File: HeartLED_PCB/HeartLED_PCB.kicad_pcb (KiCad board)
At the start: 2 copper layers, 58.8 x 52.2 mm, 38 parts, among them U1 ICM7555IBAZ-T, U2 CD4017BM96, U3 HT7750A, U4 HX SS12F44G4

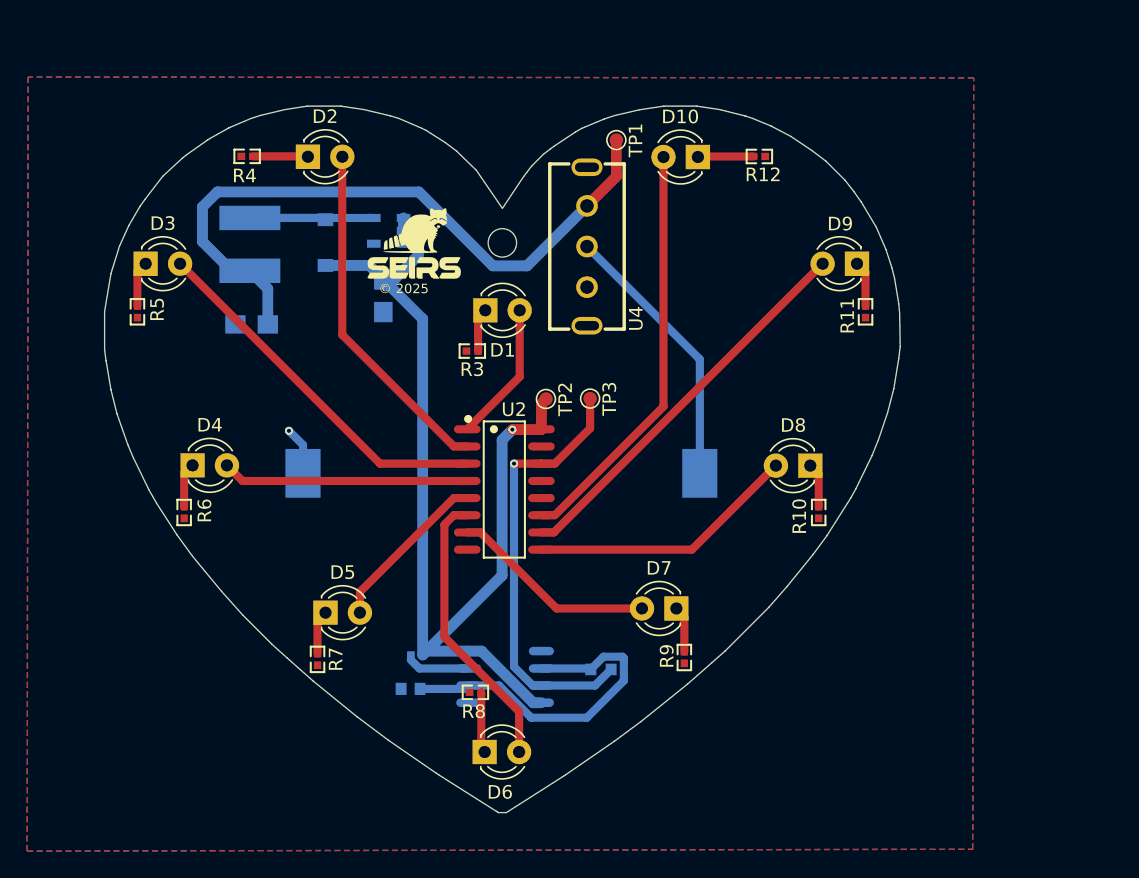
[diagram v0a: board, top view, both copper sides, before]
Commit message: Changed DC-DC Boost Converter
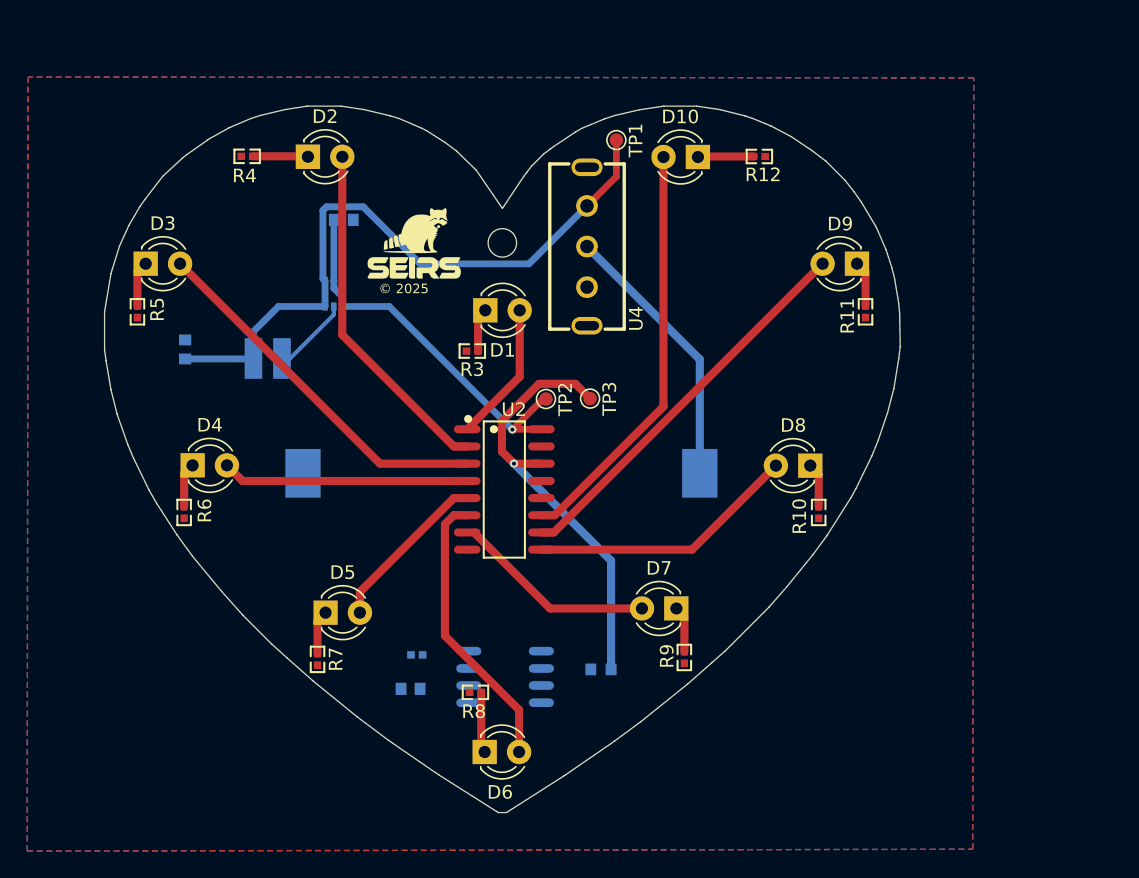
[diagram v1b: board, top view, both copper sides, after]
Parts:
- removed S1: 1N5817, FOOTPRINTS:1N5817W
- C2: value 47uF(Tantalum) -> 10uF; footprint FOOTPRINTS:TAJA476K006RNJ -> FOOTPRINTS:CL10A106MQ8NNNC
- C3: value 22uF(Tantalum) -> 10uF; footprint FOOTPRINTS:TAJA226M010RNJ -> FOOTPRINTS:CL10A106MQ8NNNC
- L1: value 47-100uH -> 4.7uH; footprint FOOTPRINTS:SMNR5040-470MT -> FOOTPRINTS:LQH3NPN4R7MMEL
- U3: value HT7750A -> TPS61222DCKR; footprint FOOTPRINTS:HT7750A -> FOOTPRINTS:TPS61222DCKR
- moved L1 8.53 mm to (112.7, 91.1), turned to 0 degrees
- moved C3 6.32 mm to (118.3, 80.9), turned to 0 degrees
- moved U3 6.16 mm to (117.6, 86.4), turned to 90 degrees
- moved C2 5.25 mm to (106.6, 90.5), turned to 90 degrees
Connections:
- U3 pad 1: +5V -> +3V
- U3 pad 3: unconnected-(U3-NC-Pad3) -> GND
- U3 pad 4: GND -> +5V
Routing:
- net +5V: track 74.7 -> 28.3 mm
- net Net-(U1-THRESHOLD): track 25.4 -> 0.00 mm
- net Net-(U3-L): track 14.6 -> 5.78 mm
- net Net-(U1-DISCHARGE): track 4.55 -> 0.00 mm
- net GND: track 3.57 -> 0.00 mm, vias 1 -> 0
- net Net-(D7-A): track 15.2 -> 14.7 mm

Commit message: Cleanup
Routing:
- net +5V: track 28.3 -> 69.5 mm
- net Net-(U1-THRESHOLD): track 0.00 -> 25.1 mm
- net Net-(U1-DISCHARGE): track 0.00 -> 5.06 mm
- net ASTABLE_OUTPUT: track 31.8 -> 36.8 mm
- net GND: track 0.00 -> 3.91 mm, vias 0 -> 1

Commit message: Cleanup
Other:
- board text added: "v1.0.0"
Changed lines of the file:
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@@
+		)
+	)
+	(gr_text "v1.0.0"
+		(at 113.34 83.12 0)
+		(layer "B.SilkS")
+		(effects
+			(font
+				(face "Liberation Mono")
+				(size 0.8 0.8)
+				(thickness 0.1)
+			)
+			(justify left mirror)
+		)
+		(render_cache "v1.0.0" 0
+			(polygon
+				(pts
+					(xy 112.947062 83.452) (xy 113.064103 83.452) (xy 113.302093 82.851748) (xy 113.191109 82.851748)
+					(xy 113.043782 83.242732) (xy 113.034403 83.272237) (xy 113.005875 83.374428) (xy 112.986727 83.309362)
+					(xy 112.965233 83.243905) (xy 112.813607 82.851748) (xy 112.703014 82.851748)
+				)
+			)
+			(polygon
+				(pts
+					(xy 112.581479 83.452) (xy 112.581479 83.372279) (xy 112.340362 83.372279) (xy 112.340362 82.814819)
+					(xy 112.366096 82.847622) (xy 112.398443 82.870398) (xy 112.436887 82.889069) (xy 112.474745 82.902832)
+					(xy 112.516984 82.913615) (xy 112.558853 82.919421) (xy 112.586559 82.920527) (xy 112.586559 82.839243)
+					(xy 112.546479 82.837033) (xy 112.507522 82.830401) (xy 112.469689 82.819349) (xy 112.432979 82.803877)
+					(xy 112.395775 82.782405) (xy 112.362558 82.755103) (xy 112.337889 82.724176) (xy 112.332156 82.714191)
+					(xy 112.240907 82.714191) (xy 112.240907 83.372279) (xy 112.04688 83.372279) (xy 112.04688 83.452)
+				)
+			)
+			(polygon
+				(pts
+					(xy 111.723112 83.452) (xy 111.723112 83.289431) (xy 111.593956 83.289431) (xy 111.593956 83.452)
+				)
+			)
+			(polygon
+				(pts
+					(xy 111.050956 83.151874) (xy 110.9218 83.151874) (xy 110.9218 83.014316) (xy 111.050956 83.014316)
+				)
+			)
+			(polygon
+				(pts
+					(xy 111.010134 82.70252) (xy 111.049905 82.707621) (xy 111.09282 82.719862) (xy 111.130487 82.73878)
+					(xy 111.162906 82.764375) (xy 111.190076 82.796647) (xy 111.208877 82.828679) (xy 111.224492 82.865424)
+					(xy 111.236919 82.906883) (xy 111.246161 82.953054) (xy 111.251259 82.993385) (xy 111.254318 83.036732)
+					(xy 111.255338 83.083095) (xy 111.254749 83.1173) (xy 111.252131 83.16047) (xy 111.247419 83.200855)
+					(xy 111.238583 83.247422) (xy 111.226475 83.289638) (xy 111.211094 83.327503) (xy 111.188318 83.367198)
+					(xy 111.175168 83.384588) (xy 111.145364 83.414236) (xy 111.110889 83.437042) (xy 111.071743 83.453007)
+					(xy 111.027926 83.462129) (xy 110.987843 83.464505) (xy 110.971392 83.464122) (xy 110.925097 83.458386)
+					(xy 110.883391 83.445767) (xy 110.846274 83.426265) (xy 110.813745 83.39988) (xy 110.785806 83.366612)
+					(xy 110.766104 83.333827) (xy 110.749742 83.296778) (xy 110.736718 83.255464) (xy 110.727035 83.209885)
+					(xy 110.721692 83.170351) (xy 110.718486 83.128088) (xy 110.717418 83.083095) (xy 110.81785 83.083095)
+					(xy 110.818009 83.101864) (xy 110.819795 83.1461) (xy 110.823565 83.186501) (xy 110.83071 83.22992)
+					(xy 110.842656 83.273595) (xy 110.858492 83.309752) (xy 110.875382 83.334919) (xy 110.906898 83.362907)
+					(xy 110.945833 83.379178) (xy 110.986671 83.383807) (xy 111.017974 83.381272) (xy 111.05867 83.367965)
+					(xy 111.091854 83.34325) (xy 111.115045 83.311706) (xy 111.122238 83.297446) (xy 111.136271 83.2584)
+					(xy 111.145233 83.218503) (xy 111.151365 83.172671) (xy 111.154313 83.129944) (xy 111.155296 83.083095)
+					(xy 111.15514 83.063372) (xy 111.153389 83.017155) (xy 111.149691 82.975357) (xy 111.142684 82.931029)
+					(xy 111.132875 82.893062) (xy 111.115436 82.852334) (xy 111.098681 82.828429) (xy 111.066775 82.801845)
+					(xy 111.026739 82.786389) (xy 110.984326 82.781993) (xy 110.957769 82.783729) (xy 110.916146 82.795606)
+					(xy 110.882468 82.818735) (xy 110.856734 82.853116) (xy 110.84762 82.872225) (xy 110.834596 82.912292)
+					(xy 110.826394 82.953348) (xy 110.821647 82.992294) (xy 110.818799 83.035543) (xy 110.81785 83.083095)
+					(xy 110.717418 83.083095) (xy 110.717989 83.048312) (xy 110.720531 83.00451) (xy 110.725106 82.963652)
+					(xy 110.733684 82.916717) (xy 110.745439 82.874381) (xy 110.760371 82.836643) (xy 110.782484 82.797429)
+					(xy 110.795316 82.780318) (xy 110.824771 82.751147) (xy 110.859283 82.728707) (xy 110.89885 82.712999)
+					(xy 110.943473 82.704023) (xy 110.984521 82.701685)
+				)
+			)
+			(polygon
+				(pts
+					(xy 110.378799 83.452) (xy 110.378799 83.289431) (xy 110.249644 83.289431) (xy 110.249644 83.452)
+				)
+			)
+			(polygon
+				(pts
+					(xy 109.706643 83.151874) (xy 109.577487 83.151874) (xy 109.577487 83.014316) (xy 109.706643 83.014316)
+				)
+			)
+			(polygon
+				(pts
+					(xy 109.665821 82.70252) (xy 109.705593 82.707621) (xy 109.748508 82.719862) (xy 109.786174 82.73878)
+					(xy 109.818593 82.764375) (xy 109.845764 82.796647) (xy 109.864565 82.828679) (xy 109.880179 82.865424)
+					(xy 109.892607 82.906883) (xy 109.901848 82.953054) (xy 109.906946 82.993385) (xy 109.910006 83.036732)
+					(xy 109.911025 83.083095) (xy 109.910436 83.1173) (xy 109.907818 83.16047) (xy 109.903106 83.200855)
+					(xy 109.89427 83.247422) (xy 109.882162 83.289638) (xy 109.866781 83.327503) (xy 109.844005 83.367198)
+					(xy 109.830855 83.384588) (xy 109.801051 83.414236) (xy 109.766576 83.437042) (xy 109.72743 83.453007)
+					(xy 109.683613 83.462129) (xy 109.643531 83.464505) (xy 109.627079 83.464122) (xy 109.580785 83.458386)
+					(xy 109.539079 83.445767) (xy 109.501961 83.426265) (xy 109.469433 83.39988) (xy 109.441493 83.366612)
+					(xy 109.421791 83.333827) (xy 109.405429 83.296778) (xy 109.392406 83.255464) (xy 109.382722 83.209885)
+					(xy 109.377379 83.170351) (xy 109.374173 83.128088) (xy 109.373105 83.083095) (xy 109.473538 83.083095)
+					(xy 109.473696 83.101864) (xy 109.475482 83.1461) (xy 109.479253 83.186501) (xy 109.486397 83.22992)
+					(xy 109.498343 83.273595) (xy 109.51418 83.309752) (xy 109.531069 83.334919) (xy 109.562585 83.362907)
+					(xy 109.601521 83.379178) (xy 109.642358 83.383807) (xy 109.673662 83.381272) (xy 109.714357 83.367965)
+					(xy 109.747541 83.34325) (xy 109.770732 83.311706) (xy 109.777926 83.297446) (xy 109.791958 83.2584)
+					(xy 109.800921 83.218503) (xy 109.807053 83.172671) (xy 109.810001 83.129944) (xy 109.810983 83.083095)
+					(xy 109.810828 83.063372) (xy 109.809076 83.017155) (xy 109.805378 82.975357) (xy 109.798371 82.931029)
+					(xy 109.788562 82.893062) (xy 109.771123 82.852334) (xy 109.754369 82.828429) (xy 109.722462 82.801845)
+					(xy 109.682426 82.786389) (xy 109.640013 82.781993) (xy 109.613457 82.783729) (xy 109.571834 82.795606)
+					(xy 109.538155 82.818735) (xy 109.512421 82.853116) (xy 109.503308 82.872225) (xy 109.490283 82.912292)
+					(xy 109.482081 82.953348) (xy 109.477335 82.992294) (xy 109.474487 83.035543) (xy 109.473538 83.083095)
+					(xy 109.373105 83.083095) (xy 109.373677 83.048312) (xy 109.376218 83.00451) (xy 109.380793 82.963652)
+					(xy 109.389371 82.916717) (xy 109.401127 82.874381) (xy 109.416059 82.836643) (xy 109.438171 82.797429)
+					(xy 109.451003 82.780318) (xy 109.480459 82.751147) (xy 109.51497 82.728707) (xy 109.554538 82.712999)
+					(xy 109.599161 82.704023) (xy 109.640209 82.701685)
+				)
+			)
 		)
 	)

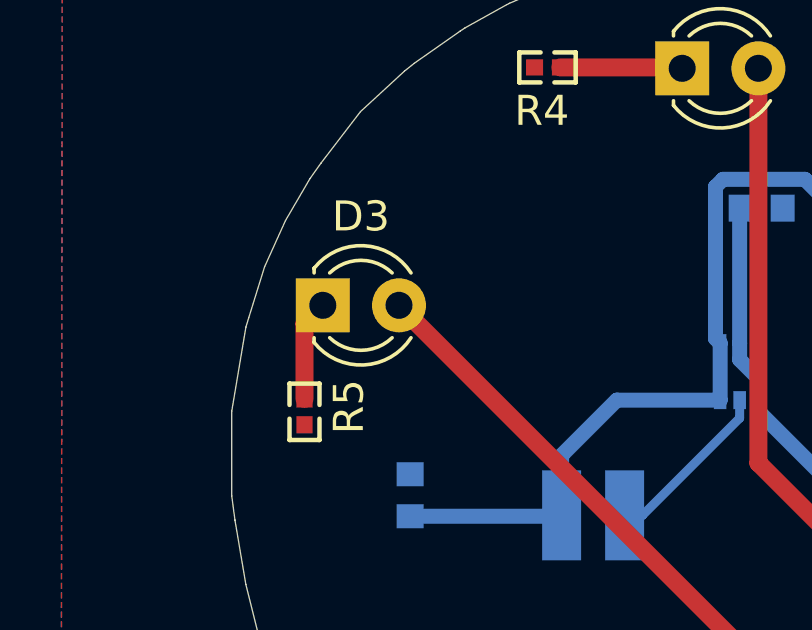
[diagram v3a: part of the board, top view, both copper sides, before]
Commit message: Changed DC-DC Boost Converter
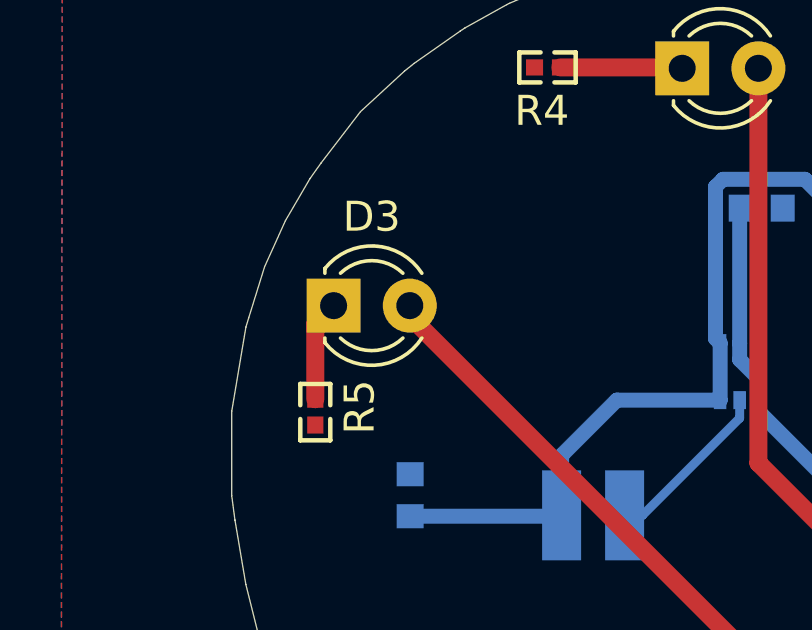
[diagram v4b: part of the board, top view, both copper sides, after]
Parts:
- moved D3 0.36 mm to (104.0, 84.2)
- moved R5 0.36 mm to (103.4, 87.7)
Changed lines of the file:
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@@
 	(footprint "LED_THT:LED_D3.0mm"
 		(layer "F.Cu")
-		(at 103.66 84.14)
+		(at 104.02 84.15)
 		(descr "LED, diameter 3.0mm, 2 pins, generated by kicad-footprint-generator")
 		(tags "LED")
@@
 	(footprint "FOOTPRINTS:0402WGJ0332TCE"
 		(layer "F.Cu")
-		(at 103.05 87.69 -90)
+		(at 103.41 87.7 -90)
 		(property "Reference" "R5"
 			(at -0.17 -1.48 90)
@@
 	)
 	(segment
-		(start 103.05 87.26)
-		(end 103.05 84.75)
+		(start 103.41 87.27)
+		(end 103.41 84.76)
 		(width 0.6)
 		(layer "F.Cu")
@@
 	)
 	(segment
-		(start 103.05 84.75)
-		(end 103.66 84.14)
+		(start 103.41 84.76)
+		(end 104.02 84.15)
 		(width 0.6)
 		(layer "F.Cu")

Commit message: Ready to route
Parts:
- removed C3: 10uF, FOOTPRINTS:CL10A106MQ8NNNC
- removed G***: LOGO, FOOTPRINTS:seirslogo
- removed G***: LOGO, FOOTPRINTS:raccoonimage
- removed H1: MountingHole, MountingHole:MountingHole_2.1mm
- removed L1: 4.7uH, FOOTPRINTS:LQH3NPN4R7MMEL
- removed R12: 3.3k, FOOTPRINTS:0402WGJ0332TCE
- removed TP2, TP3: TestPoint, TestPoint:TestPoint_Pad_D1.0mm
- removed U3: TPS61222DCKR, FOOTPRINTS:TPS61222DCKR
- removed U4: HX SS12F44G4, FOOTPRINTS:HX SS12F44G4
- added J1: Conn_01x03, Connector_PinHeader_2.54mm:PinHeader_1x03_P2.54mm_Vertical, F.Cu at (152.9, 102.6)
- added SW1: TS-1187A-B-A-B, FOOTPRINTS:TS-1187A-B-A-B, F.Cu at (150.7, 76.7)
- BT1: value Battery_Cell -> CR2032-BS-6-1; footprint Battery:BatteryHolder_Keystone_1060_1x2032 -> FOOTPRINTS:CR2032-BS-6-1; moved to F.Cu
- C1: value 4.7uF -> 100nF; footprint FOOTPRINTS:CL10A475KP8NNNC -> FOOTPRINTS:0201X104K100CT; moved to F.Cu
- C2: value 10uF -> 100nF; footprint FOOTPRINTS:CL10A106MQ8NNNC -> FOOTPRINTS:0201X104K100CT; moved to F.Cu
- D1: footprint LED_THT:LED_D3.0mm -> FOOTPRINTS:F.0603.00026_P2-0603B1TS2-06T-001
- D10, D2, D3, D4, D5, D6, D7, D8, D9: footprint LED_THT:LED_D3.0mm -> FOOTPRINTS:F.0603.00139_P2-0603R1TS2-06T-002
- R1: value 100k -> 1k; footprint FOOTPRINTS:0603WAJ0104T5E -> FOOTPRINTS:0402WGJ0102TCE; moved to F.Cu
- R10, R11, R3, R4, R5, R6, R7, R8, R9: value 3.3k -> 1k; footprint FOOTPRINTS:0402WGJ0332TCE -> FOOTPRINTS:0402WGJ0102TCE
- R2: value 10k -> 1k; footprint FOOTPRINTS:0402WGJ0103TCE -> FOOTPRINTS:0402WGJ0102TCE; moved to F.Cu
- TP1: footprint TestPoint:TestPoint_Pad_D1.0mm -> TestPoint:TestPoint_Pad_D1.5mm
- U1: value ICM7555IBAZ-T -> HX SS12F44G4; footprint FOOTPRINTS:ICM7555IBAZ-T -> FOOTPRINTS:HX SS12F44G4; moved to F.Cu
- U2: value CD4017BM96 -> ATTINY816-MN_C617908; footprint FOOTPRINTS:CD4017BM96 -> FOOTPRINTS:ATTINY816-MN
- moved C2 43.2 mm to (148.9, 81.6), turned to -90 degrees
- moved R2 42.0 mm to (130.1, 71.5), turned to 180 degrees
- moved R9 40.5 mm to (170.8, 83.3), turned to 0 degrees
- moved R7 40.1 mm to (155.8, 106.4), turned to 0 degrees
- moved R6 39.6 mm to (144.3, 114.4), turned to 0 degrees
- moved R8 39.3 mm to (164.3, 100.7), turned to 0 degrees
- moved U1 37.7 mm to (156.4, 87.6), turned to 90 degrees
- moved R1 35.3 mm to (163.8, 90.8), turned to 0 degrees
- moved D1 34.7 mm to (163.4, 89.2), turned to 180 degrees
- moved R5 34.2 mm to (131.8, 106.7), turned to 180 degrees
- moved R10 31.3 mm to (157.4, 71.5), turned to 180 degrees
- moved C1 29.3 mm to (147.0, 98.5)
- moved R4 27.4 mm to (123.3, 100.7)
- moved TP1 26.0 mm to (162.6, 84.6), turned to 0 degrees
- moved D4 16.5 mm to (123.7, 99.2)
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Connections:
- C1 pad 1: Net-(U1-THRESHOLD) -> GND
- C1 pad 2: GND -> +3V0
- C2 pad 1: +3V -> PB4
- D1 pad 2: Net-(D1-A) -> +3V0
- D10 pad 2: Net-(D10-A) -> PA4
- D2 pad 2: Net-(D2-A) -> PB1
- D3 pad 2: Net-(D3-A) -> PB0
- D4 pad 2: Net-(D4-A) -> PC0
- D5 pad 2: Net-(D5-A) -> PC1
- D6 pad 2: Net-(D6-A) -> PC2
- D7 pad 2: Net-(D7-A) -> PC3
- D8 pad 2: Net-(D8-A) -> PA1
- D9 pad 2: Net-(D9-A) -> PA2
- R1 pad 1: ASTABLE_OUTPUT -> GND
- R1 pad 2: Net-(U1-THRESHOLD) -> Net-(D1-K)
- R10 pad 1: GND -> Net-(D10-K)
- R10 pad 2: Net-(D8-K) -> GND
- R11 pad 1: GND -> +3V0
- R11 pad 2: Net-(D9-K) -> PB4
- R2 pad 1: Net-(U1-DISCHARGE) -> GND
- R2 pad 2: +5V -> Net-(D2-K)
- R3 pad 1: Net-(D1-K) -> GND
- R3 pad 2: GND -> Net-(D3-K)
- R4 pad 1: Net-(D2-K) -> GND
- R4 pad 2: GND -> Net-(D4-K)
- R5 pad 1: Net-(D3-K) -> GND
- R5 pad 2: GND -> Net-(D5-K)
- R6 pad 1: Net-(D4-K) -> GND
- R6 pad 2: GND -> Net-(D6-K)
- R7 pad 2: Net-(D5-K) -> Net-(D7-K)
- R8 pad 1: Net-(D6-K) -> GND
- R8 pad 2: GND -> Net-(D8-K)
- R9 pad 1: Net-(D7-K) -> GND
- R9 pad 2: GND -> Net-(D9-K)
- TP1 pad 1: +3V -> +3V0
- U1 pad 1: GND -> unconnected-(U1-Pad1)
- U1 pad 2: Net-(U1-THRESHOLD) -> Net-(BT1-+)
- U1 pad 3: ASTABLE_OUTPUT -> +3V0
- U1 pad 4: +5V -> unconnected-(U1-Pad4)
- U1 pad 5: GND -> unconnected-(U1-Pad5)
- U2 pad 1: Net-(D1-A) -> PA2
- U2 pad 10: Net-(D9-A) -> PB4
- U2 pad 11: Net-(D10-A) -> unconnected-(U2-PB3/TOSC1-Pad11)
- U2 pad 13: GND -> PB1
- U2 pad 14: ASTABLE_OUTPUT -> PB0
- U2 pad 15: unconnected-(U2-RESET-Pad15) -> PC0
- U2 pad 16: +5V -> PC1
- U2 pad 2: Net-(D2-A) -> unconnected-(U2-EXTCLK/PA3-Pad2)
- U2 pad 3: Net-(D3-A) -> GND
- U2 pad 4: Net-(D4-A) -> +3V0
- U2 pad 5: Net-(D5-A) -> PA4
- U2 pad 6: Net-(D6-A) -> PA5
- U2 pad 7: Net-(D7-A) -> unconnected-(U2-PA6-Pad7)
- U2 pad 8: GND -> unconnected-(U2-PA7-Pad8)
- U2 pad 9: Net-(D8-A) -> unconnected-(U2-PB5-Pad9)
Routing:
- net +5V: track 69.5 -> 0.00 mm, vias 1 -> 0
- net +3V: track 49.1 -> 0.00 mm
- net ASTABLE_OUTPUT: track 36.8 -> 0.00 mm, vias 1 -> 0
- net Net-(D10-A): track 30.8 -> 0.00 mm
- net Net-(D9-A): track 29.0 -> 0.00 mm
- net Net-(D3-A): track 27.3 -> 0.00 mm
- net Net-(D2-A): track 25.8 -> 0.00 mm
- net Net-(U1-THRESHOLD): track 25.1 -> 0.00 mm
- net Net-(D6-A): track 21.0 -> 0.00 mm
- net Net-(BT1-+): track 20.2 -> 0.00 mm
- net Net-(D8-A): track 19.9 -> 0.00 mm
- net Net-(D4-A): track 18.2 -> 0.00 mm
- net Net-(D7-A): track 14.7 -> 0.00 mm
- net Net-(D5-A): track 12.3 -> 0.00 mm
- net Net-(D1-A): track 10.4 -> 0.00 mm
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- removed copper zone on B.Cu, net GND
- removed copper zone on F.Cu, net GND
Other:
- board text removed: "Happy Valentine's Day ( ˘ ³˘)♥"
- board text removed: "github.com/ fectec/ HeartLED"
- board text removed: "v1.0.0"
- board text removed: "© 2025"

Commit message: Routed PCB
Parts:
- moved U1 10.0 mm to (163.0, 80.0)
- moved TP1 9.04 mm to (167.5, 77.0)
- moved D1 6.66 mm to (157.1, 91.3)
- moved R1 6.66 mm to (157.5, 92.9)
- moved D4 1.32 mm to (124.9, 99.6)
- moved R4 1.32 mm to (124.5, 101.2)
- moved R8 0.66 mm to (163.7, 100.7)
- moved D8 0.66 mm to (163.3, 99.1)
- moved D6 0.34 mm to (144.0, 116.9)
- moved R6 0.34 mm to (144.3, 114.1)
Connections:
- U2 pad 6: PA5 -> unconnected-(U2-PA5-Pad6)
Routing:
- net PA2: track 0.00 -> 34.3 mm
- net PB1: track 0.00 -> 33.9 mm
- net PA4: track 0.00 -> 32.6 mm
- net PB0: track 0.00 -> 31.9 mm
- net +3V0: track 0.00 -> 25.5 mm, vias 0 -> 2
- net PB4: track 0.00 -> 23.7 mm
- net PA1: track 0.00 -> 18.2 mm
- net PC0: track 0.00 -> 16.8 mm
- net PC2: track 0.00 -> 16.7 mm
- net Net-(BT1-+): track 0.00 -> 15.3 mm, vias 0 -> 1
- net PC3: track 0.00 -> 14.1 mm
- net PC1: track 0.00 -> 13.5 mm
- net UPDI: track 0.00 -> 9.60 mm
- net Net-(D6-K): track 0.00 -> 2.77 mm
- net GND: track 0.00 -> 2.11 mm
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- added copper zone on B.Cu, net +3V0
- added copper zone on F.Cu, net GND

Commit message: Added silkscreen logos
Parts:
- added G***: LOGO, FOOTPRINTS:raccoonimage, F.Cu at (137.1, 74.3)
- added G***: LOGO, FOOTPRINTS:seirslogo, F.Cu at (136.8, 77.1)
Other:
- board text added: "Happy Valentine's Day! (˃ ᵕ ˂)"
- board text added: "github.com/fectec/HeartLED"
